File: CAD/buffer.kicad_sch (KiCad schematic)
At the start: 4 parts, among them U10 SN74LVC3G34DCUR, U9 SN74LVC3G34DCUR

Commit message: new relays
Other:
- company: (none) -> NMBU-Mina
- title: (none) -> SPI-MUX
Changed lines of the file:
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@@
 (kicad_sch (version 20211123) (generator eeschema)
   (paper "A4")
+  (title_block
+    (title "SPI-MUX")
+    (date "2023-02-06")
+    (rev "0.01")
+    (company "NMBU-Mina")
+    (comment 1 "F.N.Beilegaard")
+  )
   (hierarchical_label "serial_out" (shape input) (at 146.05 129.54 0)
     (effects (font (size 1.27 1.27)) (justify left))

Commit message: Feat:Fixed digikey partnumbers, rexport, 3d mod
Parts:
- C10, C9: Digikey (none) -> CL10B104KB8NFNC; LCSC Part # (none) -> CL10B104KB8NFNC
- U10, U9: Digikey (none) -> SN74LVC3G34DCUR; LCSC Part # (none) -> SN74LVC3G34DCUR
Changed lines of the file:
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@@
+      (effects (font (size 1.27 1.27)) hide)
+    )
+    (property "Digikey" "CL10B104KB8NFNC" (id 4) (at 198.12 45.72 0)
+      (effects (font (size 1.27 1.27)) hide)
+    )
+    (property "LCSC Part #" "CL10B104KB8NFNC" (id 5) (at 198.12 45.72 0)
       (effects (font (size 1.27 1.27)) hide)
     )
@@
       (effects (font (size 1.27 1.27)) hide)
     )
+    (property "Digikey" "SN74LVC3G34DCUR" (id 4) (at 138.43 129.54 0)
+      (effects (font (size 1.27 1.27)) hide)
+    )
+    (property "LCSC Part #" "SN74LVC3G34DCUR" (id 5) (at 138.43 129.54 0)
+      (effects (font (size 1.27 1.27)) hide)
+    )
     (pin "4")
     (pin "8")
@@
       (effects (font (size 1.27 1.27)) hide)
     )
+    (property "Digikey" "SN74LVC3G34DCUR" (id 4) (at 137.16 91.44 0)
+      (effects (font (size 1.27 1.27)) hide)
+    )
+    (property "LCSC Part #" "SN74LVC3G34DCUR" (id 5) (at 137.16 91.44 0)
+      (effects (font (size 1.27 1.27)) hide)
+    )
     (pin "4")
     (pin "8")
@@
       (effects (font (size 1.27 1.27)) hide)
     )
+    (property "Digikey" "SN74LVC3G34DCUR" (id 4) (at 139.7 153.67 0)
+      (effects (font (size 1.27 1.27)) hide)
+    )
+    (property "LCSC Part #" "SN74LVC3G34DCUR" (id 5) (at 139.7 153.67 0)
+      (effects (font (size 1.27 1.27)) hide)
+    )
     (pin "4")
     (pin "8")
@@
       (effects (font (size 1.27 1.27)) hide)
     )
+    (property "Digikey" "SN74LVC3G34DCUR" (id 4) (at 137.16 104.14 0)
+      (effects (font (size 1.27 1.27)) hide)
+    )
+    (property "LCSC Part #" "SN74LVC3G34DCUR" (id 5) (at 137.16 104.14 0)
+      (effects (font (size 1.27 1.27)) hide)
+    )
     (pin "4")
     (pin "8")
@@
       (effects (font (size 1.27 1.27)) hide)
     )
+    (property "Digikey" "SN74LVC3G34DCUR" (id 4) (at 137.16 78.74 0)
+      (effects (font (size 1.27 1.27)) hide)
+    )
+    (property "LCSC Part #" "SN74LVC3G34DCUR" (id 5) (at 137.16 78.74 0)
+      (effects (font (size 1.27 1.27)) hide)
+    )
     (pin "4")
     (pin "8")
@@
       (effects (font (size 1.27 1.27)) hide)
     )
+    (property "Digikey" "SN74LVC3G34DCUR" (id 4) (at 138.43 142.24 0)
+      (effects (font (size 1.27 1.27)) hide)
+    )
+    (property "LCSC Part #" "SN74LVC3G34DCUR" (id 5) (at 138.43 142.24 0)
+      (effects (font (size 1.27 1.27)) hide)
+    )
     (pin "4")
     (pin "8")
@@
       (effects (font (size 1.27 1.27)) hide)
     )
+    (property "Digikey" "CL10B104KB8NFNC" (id 4) (at 180.34 46.99 0)
+      (effects (font (size 1.27 1.27)) hide)
+    )
+    (property "LCSC Part #" "CL10B104KB8NFNC" (id 5) (at 180.34 46.99 0)
+      (effects (font (size 1.27 1.27)) hide)
+    )

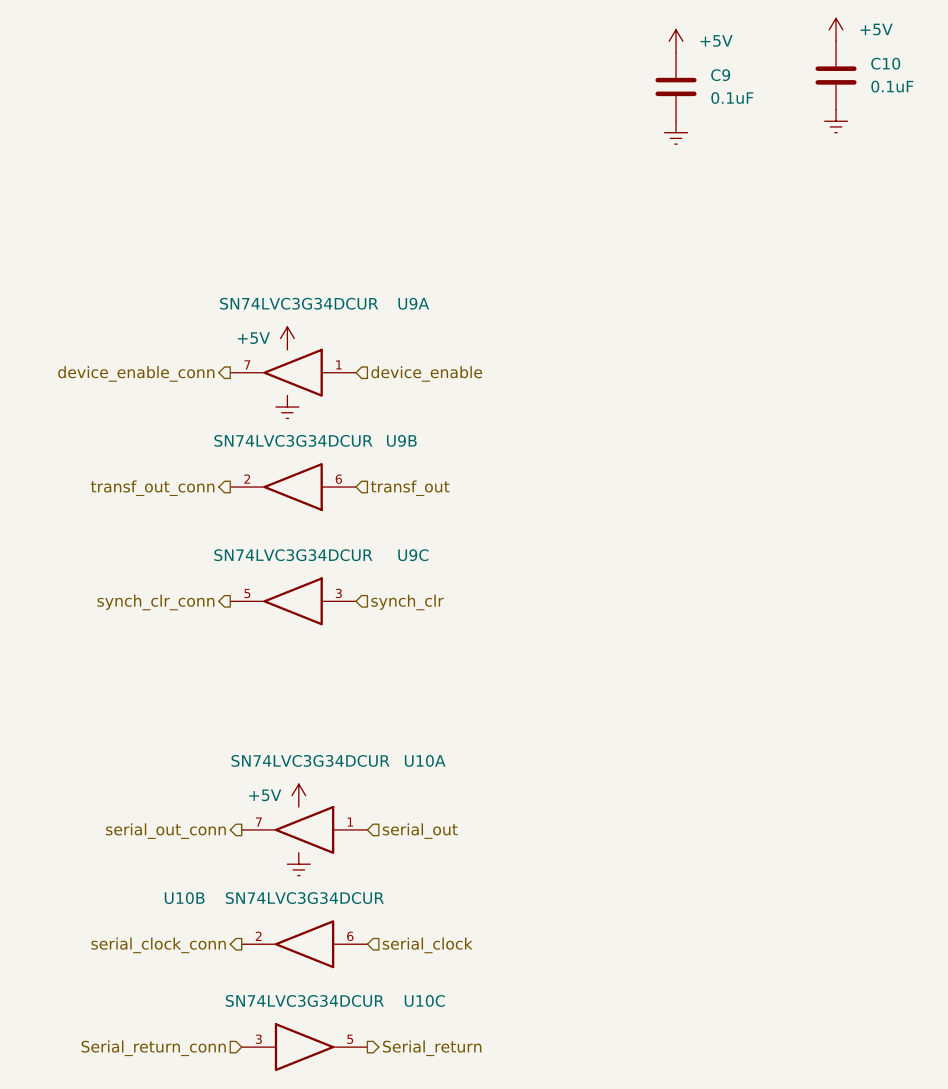
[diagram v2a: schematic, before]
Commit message: Feat: Single side test
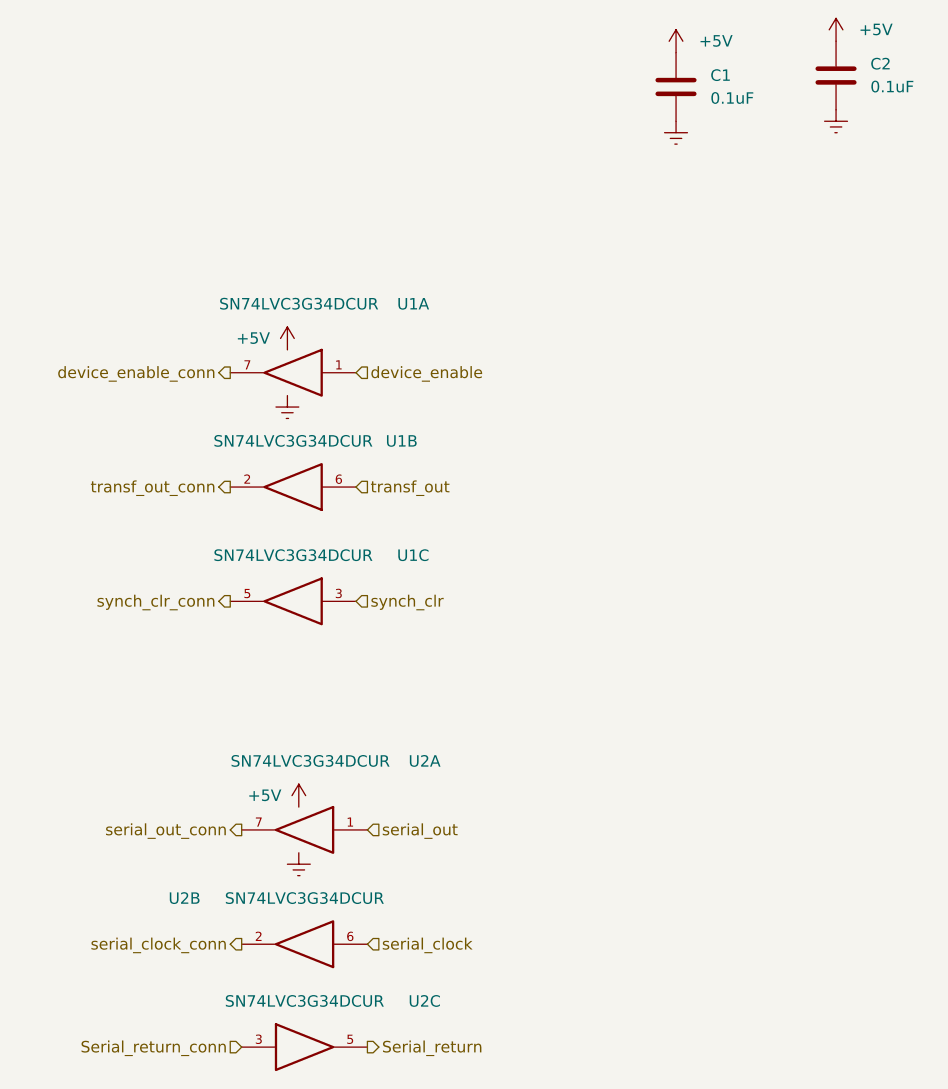
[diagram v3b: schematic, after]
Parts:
- renumbered C9 to C1, C10 to C2, U9 to U1, U10 to U2
